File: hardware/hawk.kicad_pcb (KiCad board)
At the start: 2 copper layers, 41 x 41 mm, 44 parts, among them J1 UART2, J2 SWD, J3 54-00298, SW1 EVQ-P7L01P, U1 MIC5504-3.3YM5, U2 STM32G431K6Tx, U3 MAX9860ETG+T, U4 MIC5504-1.8YM5

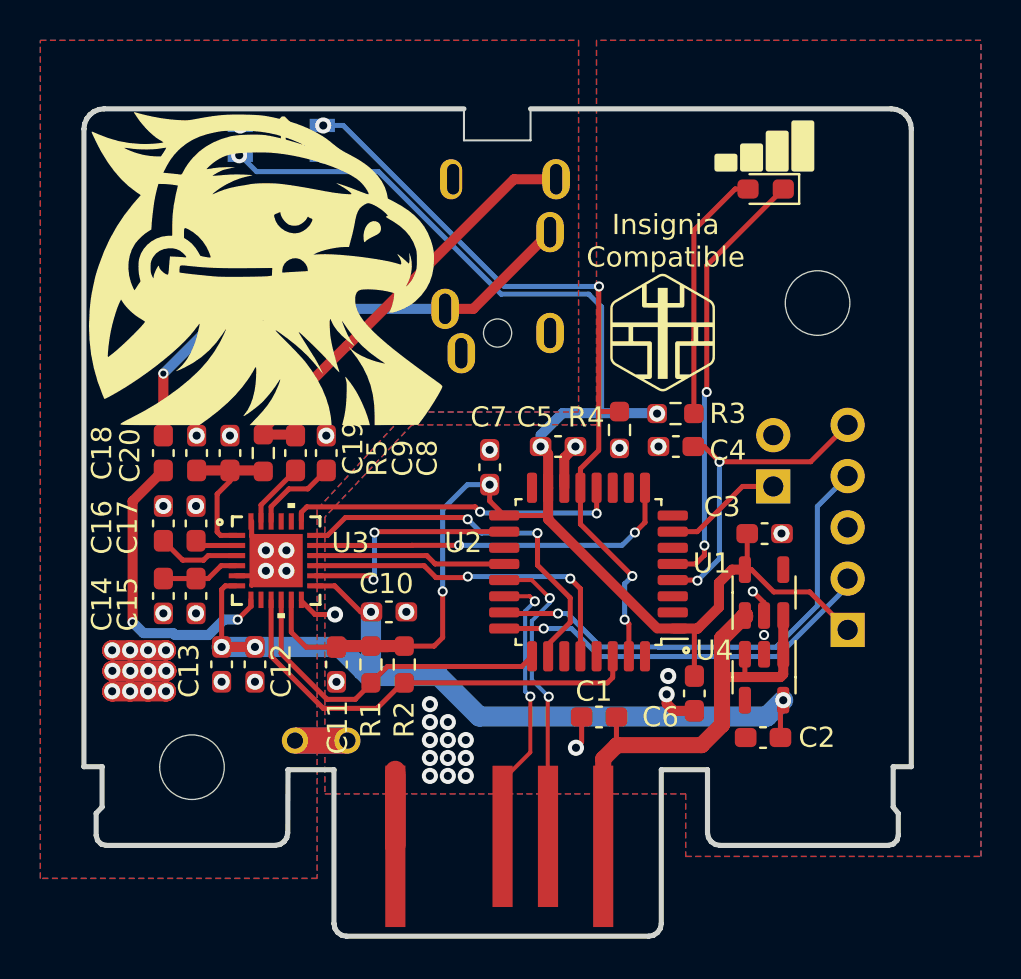
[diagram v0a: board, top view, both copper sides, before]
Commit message: hardware: Tweak to TRRS footprint
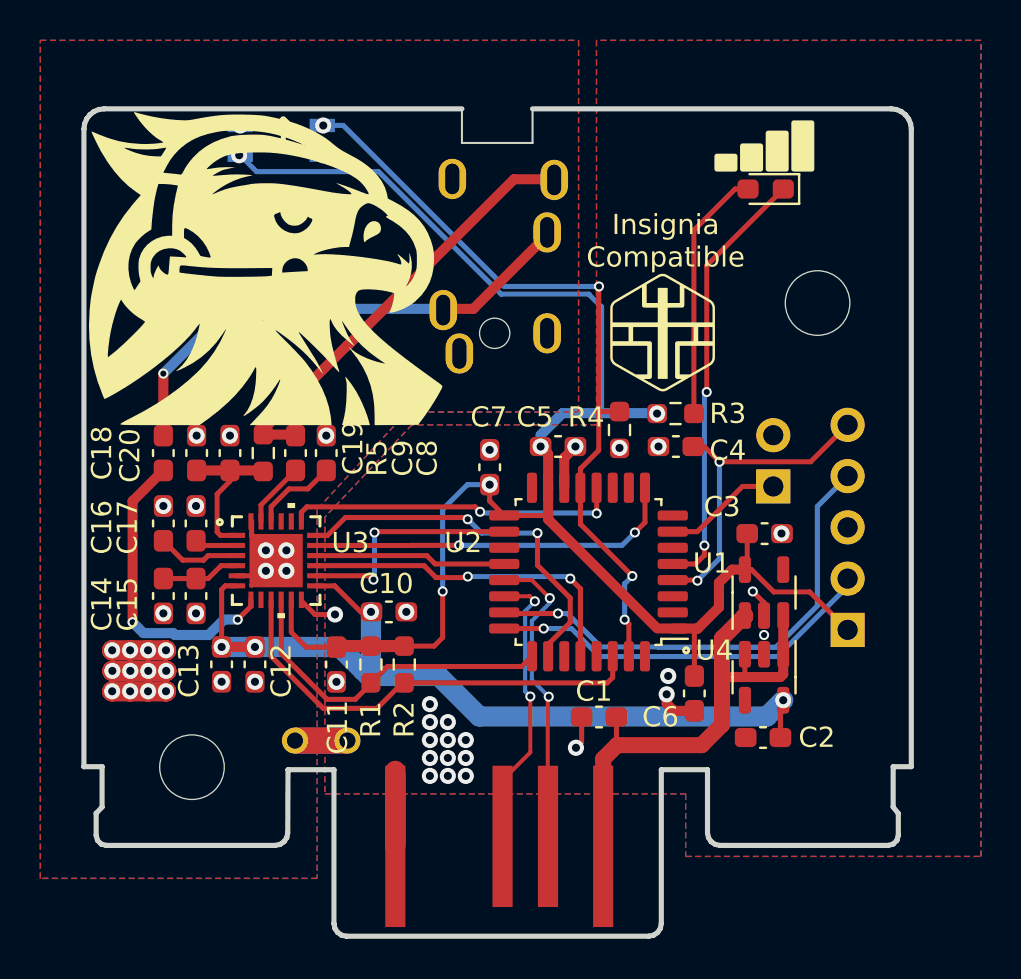
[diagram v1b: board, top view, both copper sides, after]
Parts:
- moved J3 2.18 mm to (148.5, 82.5)
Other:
- outline, holes or cut-outs redrawn
